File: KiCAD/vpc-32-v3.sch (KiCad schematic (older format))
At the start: 81 parts, among them J1 BARREL_JACK, J2 PIC32_ICSP, J3 keyboard, J4 SD_Card, J5 VGA out, J6 PIC12_ICSP, J7 RJ12, Q1 2N3904, Q2 2N3906, SW1 SPDT, U1 LM340T5, U2 PIC12F1572, U3 LM1117-3.3, U4 PIC32MX170F256B, U5 LM386, U6 MCP7940N, U7 23LC512, Y1 10Mhz, Y2 32,768Hz, sw1 reset

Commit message: 2018-01-31 ---------- 1. Modification schématique. Déplacement des signaux SCL de l'interface I2C sur broche RB0 (pin 4) et déplacement cathode power LED sur BP14 (pin 25)
2018-01-30
----------
1. Travail sur RTCC.c
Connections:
- net SCL: no longer U4.25 (PB14)
- net ~power: now also U4.25 (PB14)
- net PGED renamed PGED/SCL
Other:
- note added: "révision 2018-01-31, 11:09\n"
- note removed: "révision 2018-01-29, 11:50"
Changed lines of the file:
@@
 P 3900 3500
 F 0 "C6" H 3925 3600 50  0000 L CNN
-F 1 "100nF" H 3925 3400 50  0000 L CNN
+F 1 "100nF" H 3650 3425 50  0000 L CNN
 F 2 "" H 3938 3350 50  0001 C CNN
 F 3 "" H 3900 3500 50  0001 C CNN
@@
 VSync
 Text Label 4475 3650 2    39   ~ 0
-PGED
+PGED/SCL
 Text Label 4475 3750 2    39   ~ 0
 PGEC/alarm
@@
 Wire Wire Line
 	7050 1775 7450 1775
-Text Label 6075 3650 0    39   ~ 0
-SCL
 $Comp
 L R R17
@@
 $EndComp
 Text Notes 7000 7125 0    60   ~ 0
-révision  2018-01-29, 11:50
+révision  2018-01-31, 11:09\n
 $Comp
 L C C20
@@
 Wire Wire Line
 	8400 2625 8375 2625
+Text Label 6075 3650 0    39   ~ 0
+~power
 $EndSCHEMATC

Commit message: 2018-02-02 ---------- 1.  Correction erreur schématique. 2.  Travail sur rtcc.c interface I2C
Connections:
- net SCL: now also R19.2, U6.6 (SCL); no longer R18.2, U6.5 (SDA)
- net SDA: now also R18.2, U6.5 (SDA); no longer R19.2, U6.6 (SCL)
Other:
- note added: "révision 2018-02-02, 21:44\n\n"
- note removed: "révision 2018-01-31, 11:09\n"
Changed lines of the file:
@@
 Text Label 4475 3550 2    39   ~ 0
 SDA
-Text Label 6550 2550 2    39   ~ 0
+Text Label 6550 2650 2    39   ~ 0
 SDA
 Text Label 6550 2850 2    39   ~ 0
 alarm
-Text Label 6550 2650 2    39   ~ 0
+Text Label 6550 2550 2    39   ~ 0
 SCL
 Text Label 2775 2600 0    39   ~ 0
@@
 	1    0    0    -1
 $EndComp
-Text Notes 8150 6850 0    60   ~ 0
+Text Notes 7100 6750 0    79   ~ 0
 Jacques Deschênes, Copyright 2018
 $Comp
@@
 	-1   0    0    1
 $EndComp
-Text Notes 7000 7125 0    60   ~ 0
-révision  2018-01-31, 11:09\n
+Text Notes 7000 7125 0    79   ~ 0
+révision  2018-02-02, 21:44\n\n
 $Comp
 L C C20

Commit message: 2018-02-03 ----------- 1. Modification schématique ajout filtre sur alimentation du MCP7940N. 2. Travail sur interface I2C. Interface maintenant fonctionnelle.
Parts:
- added C13: 100nF, symbol C
- added C9: 1µF, symbol C
- added L1: 1µH, symbol L
- renumbered C18 to C10, C9 to C11, C10 to C12, C11 to C14, C12 to C15, C13 to C16, C14 to C17, C15 to C18, C16 to C19, C17 to C20, C19 to C21, C20 to C22, C21 to C23, C22 to C24, C23 to C25, L1 to L2, R16 to R15, R15 to R16
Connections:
- net GND: now also C13.2, C9.2
- net Vdd: now also C9.1, L1.2; no longer C10.1, R17.1, R18.1, R19.1, U6.8 (VCC)
- new net: C10.1, C13.1, L1.1, R17.1, R18.1, R19.1, U6.8 (VCC)
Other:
- note added: "révision 2018-02-03, 11:03\n\n\n"
- note removed: "révision 2018-02-02, 21:44\n\n"
- moved on the sheet: C10, D6, R15

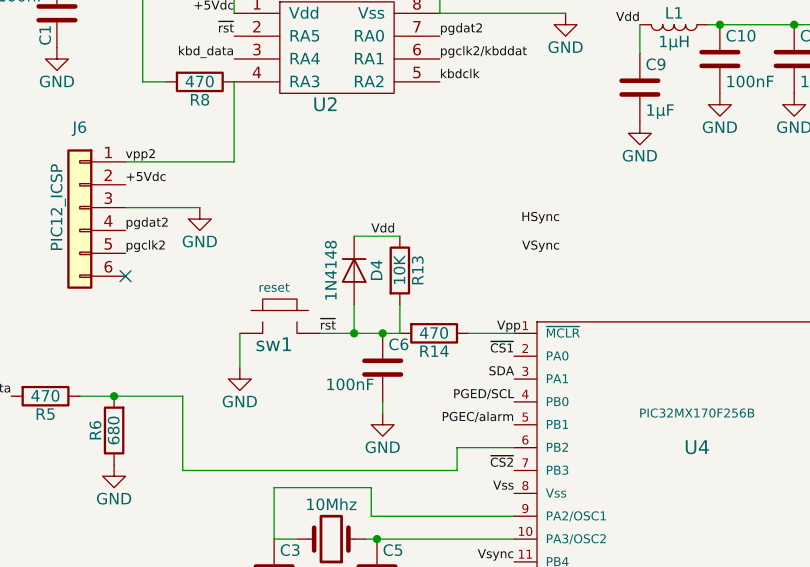
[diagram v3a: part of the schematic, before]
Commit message: réécris console:read_line() Corrigé bogue dans shell:next_token()
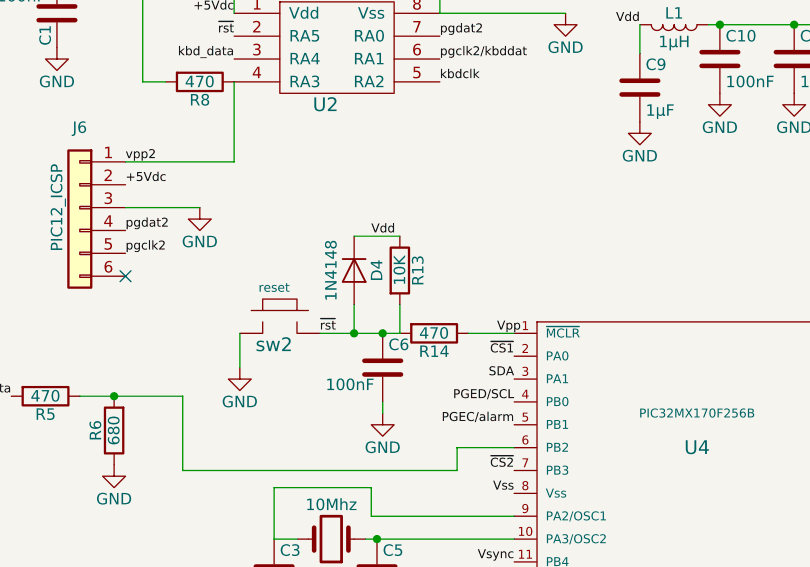
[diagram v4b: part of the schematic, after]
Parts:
- renumbered sw1 to sw2
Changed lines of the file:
@@
 Text Label 6075 4650 0    39   ~ 0
 video
-Text Label 4675 2875 2    39   ~ 0
-HSync
-Text Label 4675 3000 2    39   ~ 0
-VSync
 $Comp
 L SD_Card J4
@@
 $EndComp
 $Comp
-L push_button sw1
+L push_button sw2
 U 1 1 5A6EA9E3
 P 3425 3250
-F 0 "sw1" H 3425 3100 60  0000 C CNN
+F 0 "sw2" H 3425 3100 60  0000 C CNN
 F 1 "reset" H 3425 3350 39  0000 C CNN
 F 2 "" H 3425 3250 60  0001 C CNN

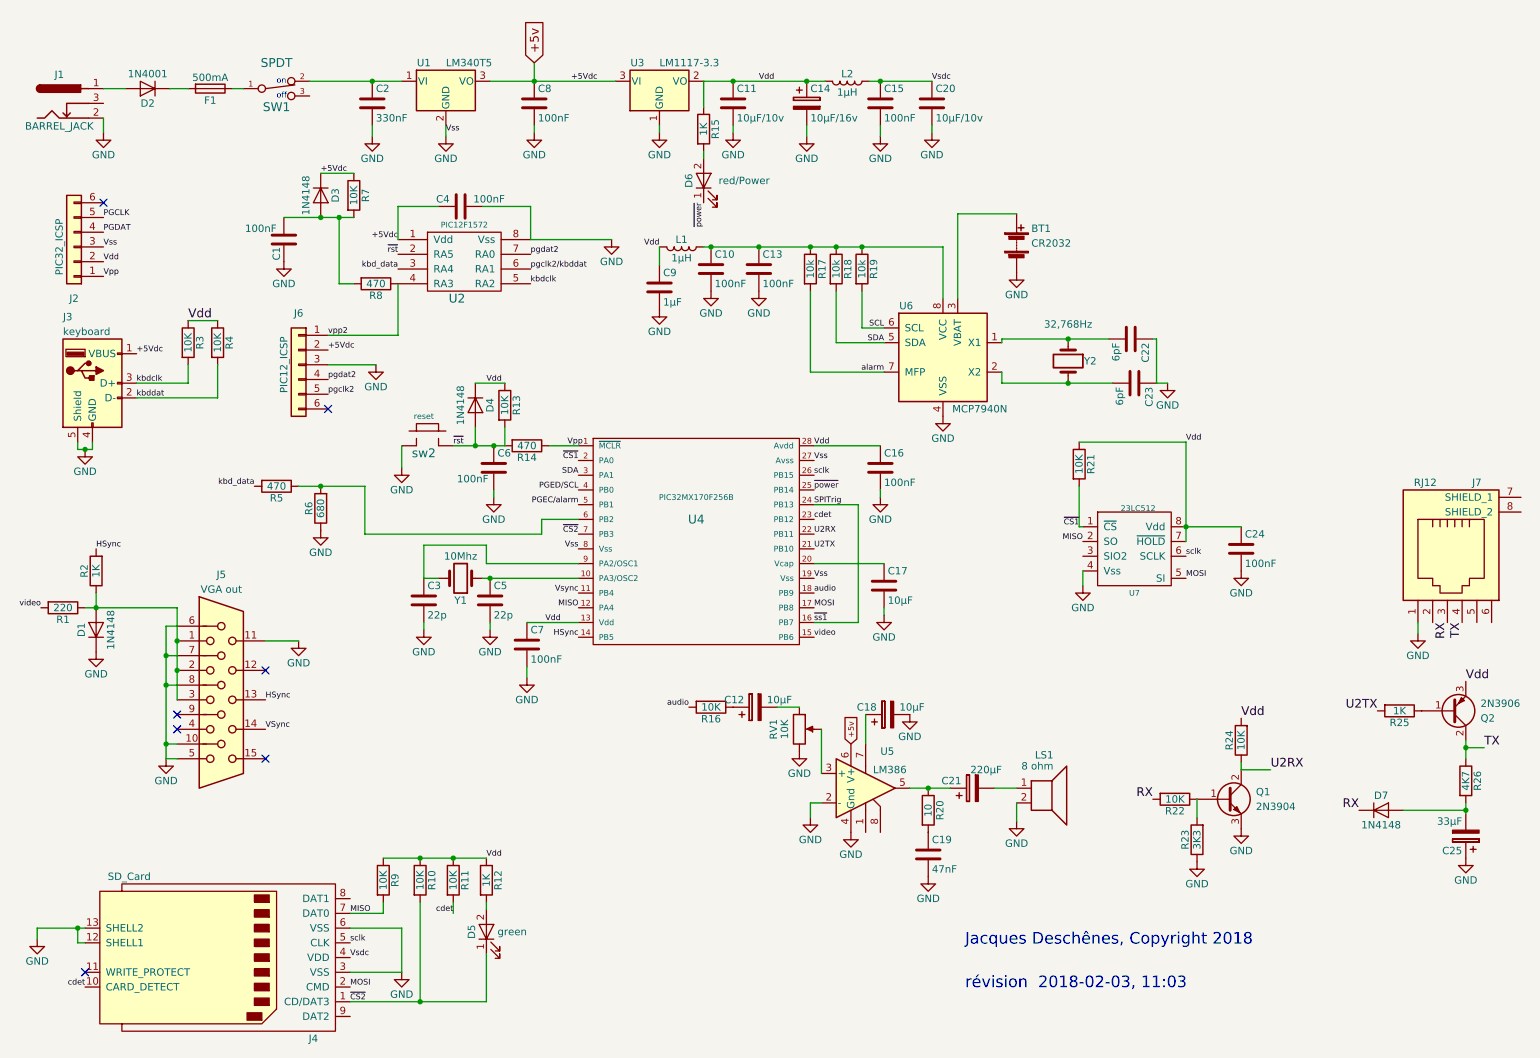
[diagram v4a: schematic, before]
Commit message: 1. Continuer travail sur xmodem.c 2. Ajout d'un inverseur de tension dans le circuit. Nécessaire pour RS-232. 3. Agrandissement du tampon réception COM à 128 octets dans serial_comm.c 4. Ajout de la fonction flow_control() dans serial_comm.c 4. xmodem.c complété
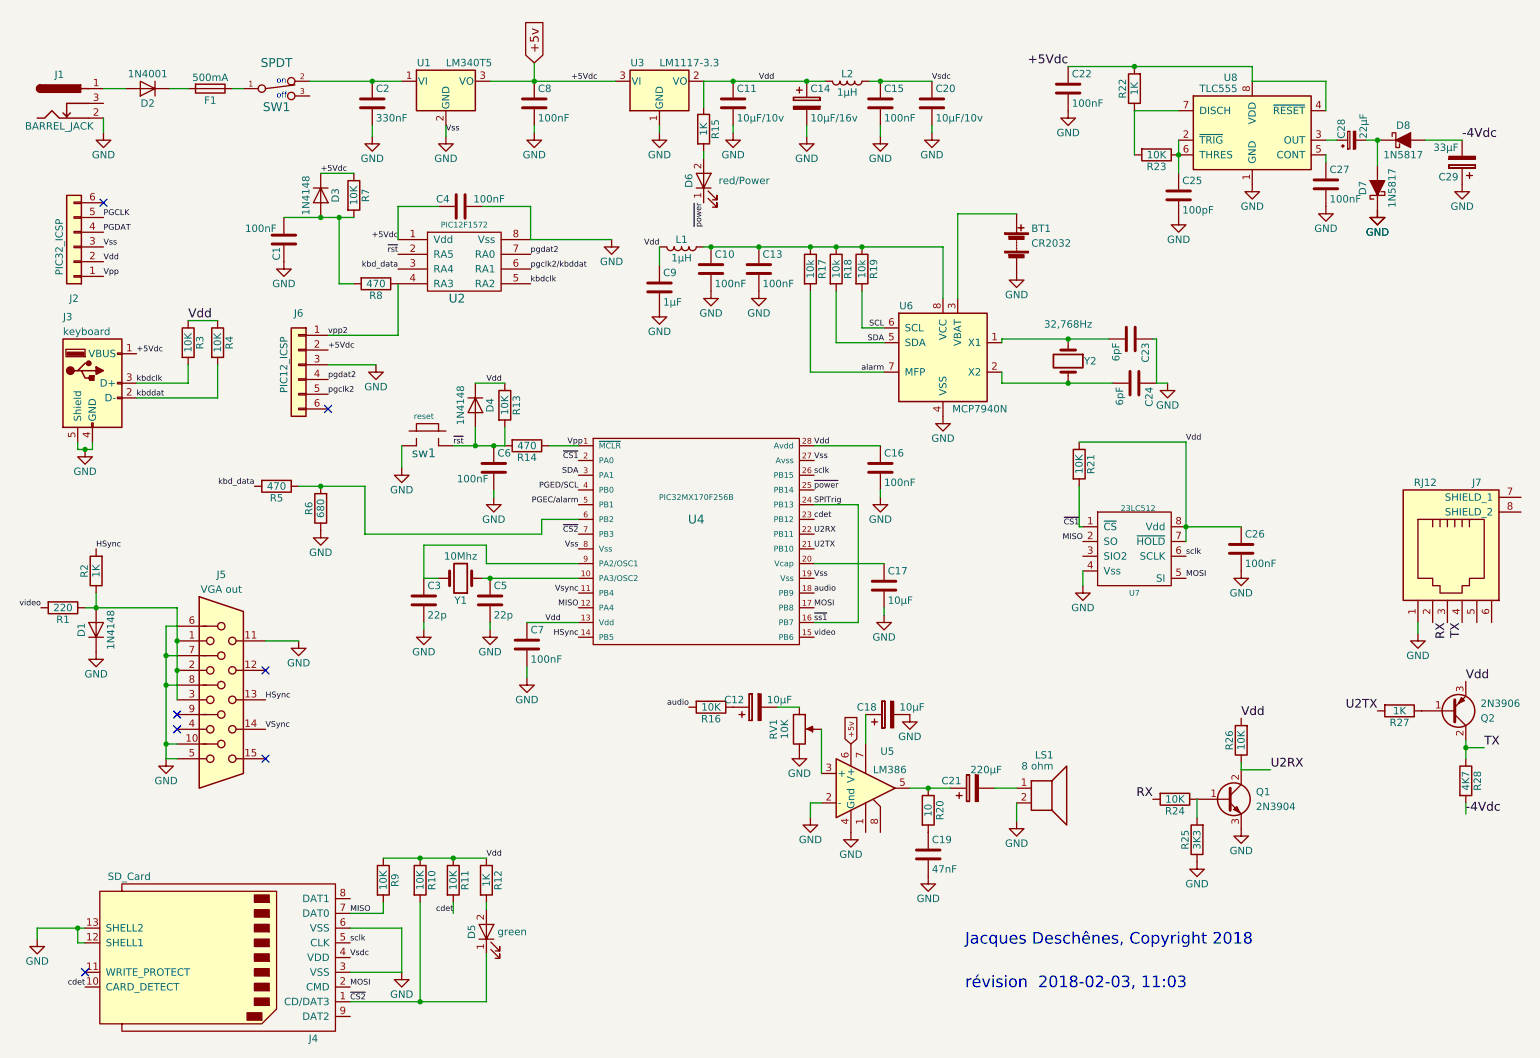
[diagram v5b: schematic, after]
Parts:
- removed D7: 1N4148, symbol D
- added C22, C27: 100nF, symbol C
- added C25: 100pF, symbol C
- added C28: 22µF, symbol CP_Small
- added D7, D8: 1N5817, symbol D_Schottky_ALT
- added R22: 1K, symbol R
- added R23: 10K, symbol R
- added U8: TLC555, symbol TLC555
- renumbered C22 to C23, C23 to C24, C24 to C26, C25 to C29, R22 to R24, R23 to R25, R24 to R26, R25 to R27, R26 to R28, sw2 to sw1
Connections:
- net +5v: now also C22.1, R22.2, U8.4 (~RESET), U8.8 (VDD)
- net GND: now also C22.2, C25.2, C27.2, D7.1 (K), U8.1 (GND)
- net -4Vdc: now reaches C29.2, R28.2
- net -4Vdc: now also D8.2 (A)
- new net: C25.1, R23.1, U8.2 (~TRIG), U8.6 (THRES)
- new net: C28.1, U8.3 (OUT)
- new net: C27.1, U8.5 (CONT)
- new net: R22.1, R23.2, U8.7 (DISCH)
- new net: C28.2, D7.2 (A), D8.1 (K)
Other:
- moved on the sheet: C29
